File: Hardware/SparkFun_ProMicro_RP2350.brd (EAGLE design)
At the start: 17.8 x 33 mm, 124 parts, among them J2 QWIIC_RIGHT_ANGLE, J5 USB Female Type C Connector, U1 RT9080-33GJ5, U2 RP2350A, U3 WS2812_2020, U4 W25QXX128MBIT, U5 APS6404L-3SQR-ZR, Y1 12MHz

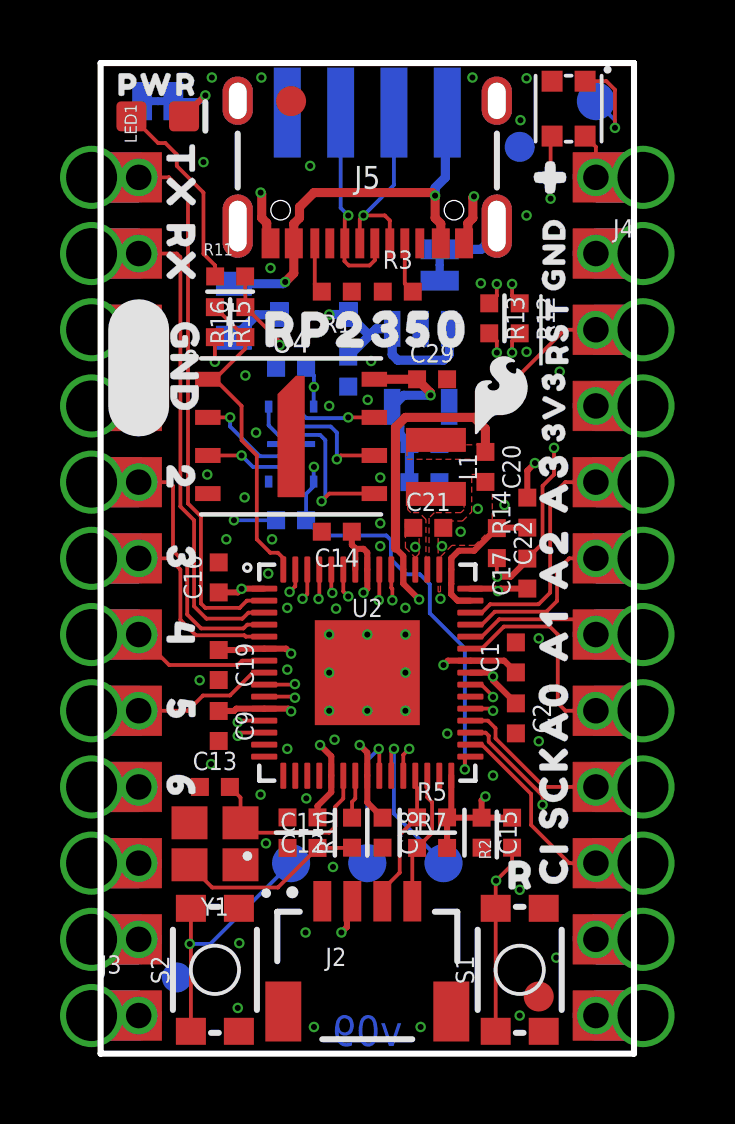
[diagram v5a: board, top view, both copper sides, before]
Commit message: Design review updates
Change version number to v02 instead of jumping to v09
Add PROD_ID to PSRAM
Nudge BOOT trace away from UART trace on adjacent layer
Fix "2" silk on bottom
Nudge C13 away from "6" silk on top
Fix acid trap on pad 5 of U1
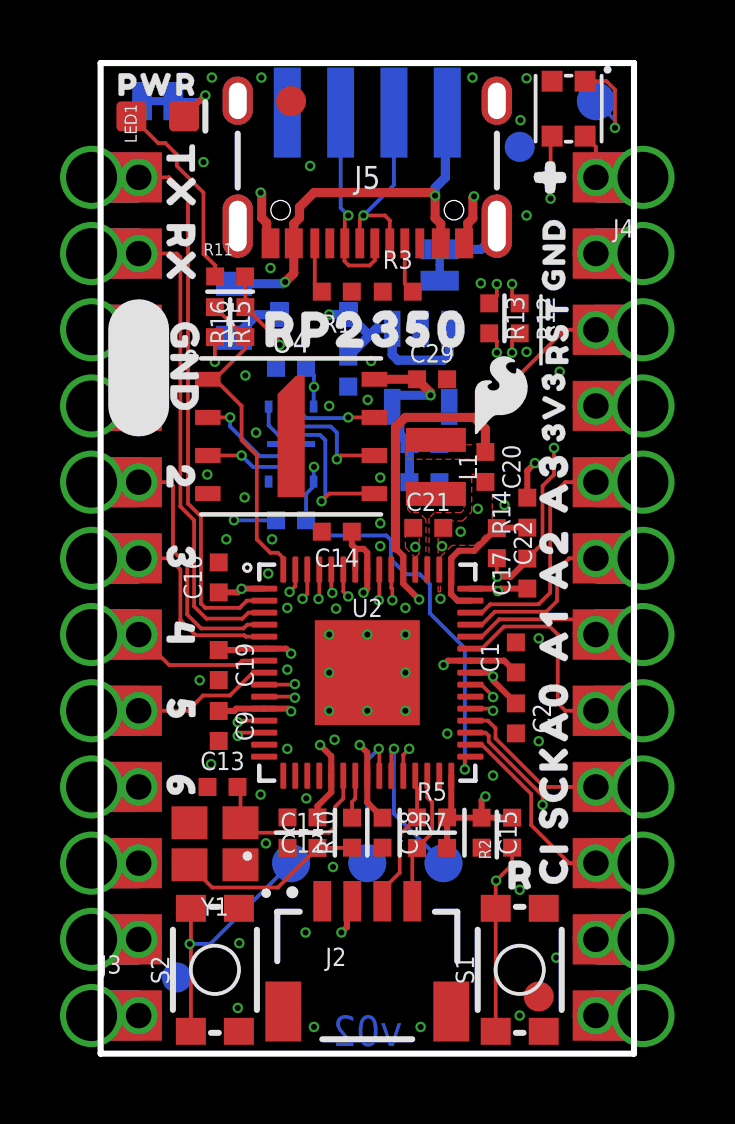
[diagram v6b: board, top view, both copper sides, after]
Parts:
- moved U$23 1.27 mm to (2.92, 19.1)
- moved C13 0.25 mm to (4.06, 8.89)
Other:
- board text added: "v02"
- board text removed: "v09"
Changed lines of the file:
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@@
 <wire x1="17.78" y1="0" x2="17.78" y2="33.02" width="0.2032" layer="20"/>
 <wire x1="17.78" y1="33.02" x2="0" y2="33.02" width="0.2032" layer="20"/>
-<text x="8.89" y="0.762" size="1.016" layer="16" font="vector" ratio="25" rot="MR0" align="center">v09</text>
+<text x="8.89" y="0.762" size="1.016" layer="16" font="vector" ratio="25" rot="MR0" align="center">v02</text>
 <wire x1="1.27" y1="24.13" x2="1.27" y2="21.59" width="2.032" layer="21"/>
 <wire x1="1.27" y1="24.13" x2="1.27" y2="21.59" width="2.032" layer="22"/>
@@
 <attribute name="VALUE" x="6.731" y="6.296" size="0.6096" layer="27" font="vector" ratio="20" align="top-center"/>
 </element>
-<element name="C13" library="SparkFun-Capacitors" package="0402-TIGHT" value="15pF" x="3.81" y="8.89" smashed="yes">
-<attribute name="NAME" x="3.81" y="9.452" size="0.6096" layer="25" font="vector" ratio="20" align="bottom-center"/>
-<attribute name="PROD_ID" value="CAP-13063" x="5.08" y="25.4" size="1.778" layer="27" font="vector" ratio="15" display="off"/>
-<attribute name="VALUE" x="3.81" y="8.328" size="0.6096" layer="27" font="vector" ratio="20" align="top-center"/>
+<element name="C13" library="SparkFun-Capacitors" package="0402-TIGHT" value="15pF" x="4.064" y="8.89" smashed="yes">
+<attribute name="NAME" x="4.064" y="9.452" size="0.6096" layer="25" font="vector" ratio="20" align="bottom-center"/>
+<attribute name="PROD_ID" value="CAP-13063" x="5.334" y="25.4" size="1.778" layer="27" font="vector" ratio="15" display="off"/>
+<attribute name="VALUE" x="4.064" y="8.328" size="0.6096" layer="27" font="vector" ratio="20" align="top-center"/>
 </element>
 <element name="R10" library="SparkFun-Resistors" package="0402-TIGHT" value="1k" x="8.382" y="7.366" smashed="yes" rot="R90">
@@
 <element name="U$21" library="output" package="RX1" value="" x="3.175" y="26.416" smashed="yes" rot="MR270"/>
 <element name="U$22" library="output" package="GND2" value="" x="3.175" y="22.86" smashed="yes" rot="MR270"/>
-<element name="U$23" library="output" package="20" value="" x="2.921" y="20.32" smashed="yes" rot="MR0"/>
+<element name="U$23" library="output" package="20" value="" x="2.921" y="19.05" smashed="yes" rot="MR0"/>
 <element name="U$24" library="output" package="31" value="" x="2.921" y="16.51" smashed="yes" rot="MR0"/>
 <element name="U$25" library="output" package="42" value="" x="2.921" y="13.97" smashed="yes" rot="MR0"/>
@@
 <element name="FRAME2" library="SparkFun-Aesthetics" package="CREATIVE_COMMONS" value="FRAME-LEDGER" x="39.37" y="-7.62" smashed="yes">
 <attribute name="DESIGNER" value="Dryw Wade" x="39.37" y="-7.62" size="1.778" layer="27" font="vector" ratio="15" display="off"/>
-<attribute name="REV" value="v09" x="39.37" y="-7.62" size="1.778" layer="27" font="vector" ratio="15" display="off"/>
+<attribute name="REV" value="v02" x="39.37" y="-7.62" size="1.778" layer="27" font="vector" ratio="15" display="off"/>
 </element>
 <element name="U$4" library="output" package="PRO_MICRO0" value="" x="10.668" y="12.954" smashed="yes" rot="MR270"/>
@@
 <element name="U5" library="RP2350A" package="APS6404L-3SQR-ZR" value="APS6404L-3SQR-ZR" x="6.35" y="20.32" smashed="yes" rot="MR90">
 <attribute name="NAME" x="8.35" y="20.32" size="0.5" layer="26" font="vector" ratio="15" rot="MR90" align="center"/>
+<attribute name="PROD_ID" value="IC-21870" x="6.35" y="20.32" size="1.778" layer="28" rot="MR90" display="off"/>
 <attribute name="VALUE" x="4.35" y="20.32" size="0.5" layer="28" font="vector" ratio="15" rot="MR90" align="center"/>
 </element>
@@
 <wire x1="10.9982" y1="22.0298" x2="10.9982" y2="21.9456" width="0.3048" layer="1"/>
 <via x="10.9982" y="21.9456" extent="1-16" drill="0.2"/>
-<wire x1="9.718" y1="21.5599" x2="10.1037" y2="21.9456" width="0.3048" layer="16"/>
-<wire x1="10.1037" y1="21.9456" x2="10.9982" y2="21.9456" width="0.3048" layer="16"/>
+<wire x1="9.718" y1="21.5599" x2="9.718" y2="21.9456" width="0.3048" layer="16"/>
+<wire x1="9.718" y1="21.9456" x2="10.9982" y2="21.9456" width="0.3048" layer="16"/>
 <wire x1="4.826" y1="24.884" x2="5.969" y2="23.741" width="0.127" layer="1"/>
 <wire x1="5.969" y1="23.741" x2="5.969" y2="23.622" width="0.127" layer="1"/>
@@
 <wire x1="4.993" y1="7.366" x2="7.62" y2="7.366" width="0.127" layer="1"/>
 <wire x1="7.62" y1="7.366" x2="7.8233" y2="7.5693" width="0.127" layer="1"/>
-<wire x1="4.664" y1="7.695" x2="4.664" y2="8.536" width="0.127" layer="1"/>
-<wire x1="4.664" y1="8.536" x2="4.31" y2="8.89" width="0.127" layer="1"/>
+<wire x1="4.664" y1="7.695" x2="4.664" y2="8.79" width="0.127" layer="1"/>
+<wire x1="4.664" y1="8.79" x2="4.564" y2="8.89" width="0.127" layer="1"/>
 </signal>
 <signal name="X1B">
@@
 <vertex x="10.2108" y="19.812"/>
 <vertex x="13.0302" y="19.812"/>
-<vertex x="13.0302" y="19.812"/>
 <vertex x="13.0302" y="20.2946"/>
 <vertex x="12.0396" y="20.2946"/>
@@
 <wire x1="3.01" y1="3.6194" x2="2.9718" y2="3.6576" width="0.127" layer="1"/>
 <via x="2.9718" y="3.6576" extent="1-16" drill="0.2"/>
-<wire x1="2.8448" y1="22.098" x2="2.8448" y2="3.7846" width="0.127" layer="2"/>
-<wire x1="2.8448" y1="3.7846" x2="2.9718" y2="3.6576" width="0.127" layer="2"/>
+<wire x1="2.8448" y1="22.098" x2="2.8448" y2="11.9126" width="0.127" layer="2"/>
+<wire x1="2.9718" y1="11.7856" x2="2.9718" y2="3.6576" width="0.127" layer="2"/>
+<wire x1="2.9718" y1="11.7856" x2="2.8448" y2="11.9126" width="0.127" layer="2"/>
 <wire x1="2.8448" y1="22.098" x2="3.81" y2="23.0632" width="0.127" layer="2"/>
 <via x="3.81" y="23.0632" extent="1-16" drill="0.2"/>

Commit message: Bump version number to v10
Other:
- board text added: "v10"
- board text removed: "v02"
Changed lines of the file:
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@@
 <wire x1="17.78" y1="0" x2="17.78" y2="33.02" width="0.2032" layer="20"/>
 <wire x1="17.78" y1="33.02" x2="0" y2="33.02" width="0.2032" layer="20"/>
-<text x="8.89" y="0.762" size="1.016" layer="16" font="vector" ratio="25" rot="MR0" align="center">v02</text>
+<text x="8.89" y="0.762" size="1.016" layer="16" font="vector" ratio="25" rot="MR0" align="center">v10</text>
 <wire x1="1.27" y1="24.13" x2="1.27" y2="21.59" width="2.032" layer="21"/>
 <wire x1="1.27" y1="24.13" x2="1.27" y2="21.59" width="2.032" layer="22"/>
@@
 <element name="FRAME2" library="SparkFun-Aesthetics" package="CREATIVE_COMMONS" value="FRAME-LEDGER" x="39.37" y="-7.62" smashed="yes">
 <attribute name="DESIGNER" value="Dryw Wade" x="39.37" y="-7.62" size="1.778" layer="27" font="vector" ratio="15" display="off"/>
-<attribute name="REV" value="v02" x="39.37" y="-7.62" size="1.778" layer="27" font="vector" ratio="15" display="off"/>
+<attribute name="REV" value="v10" x="39.37" y="-7.62" size="1.778" layer="27" font="vector" ratio="15" display="off"/>
 </element>
 <element name="U$4" library="output" package="PRO_MICRO0" value="" x="10.668" y="12.954" smashed="yes" rot="MR270"/>
